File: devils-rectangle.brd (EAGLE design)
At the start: 54 x 54 mm, 26 parts, among them J3 CORTEX_DEBUG_PTH, J6 USB-MICROB, U1 ATSAMD21G-M, U2 MIC5501-3.0YM5-TR, U3 TPD2S017, Y1 32.768KHZ

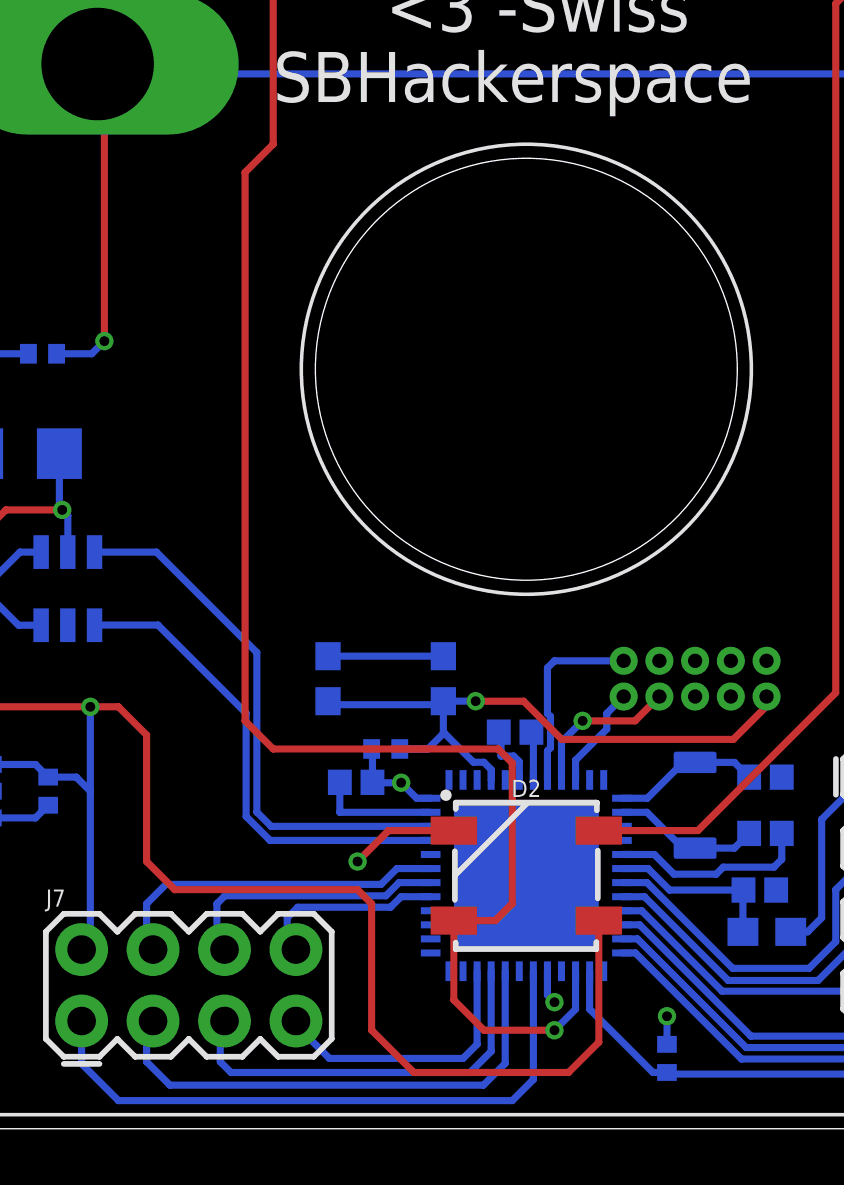
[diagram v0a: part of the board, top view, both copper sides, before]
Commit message: resolved routing errors
resolved routing errors, added crystal, and tested. submitted to oshpark.
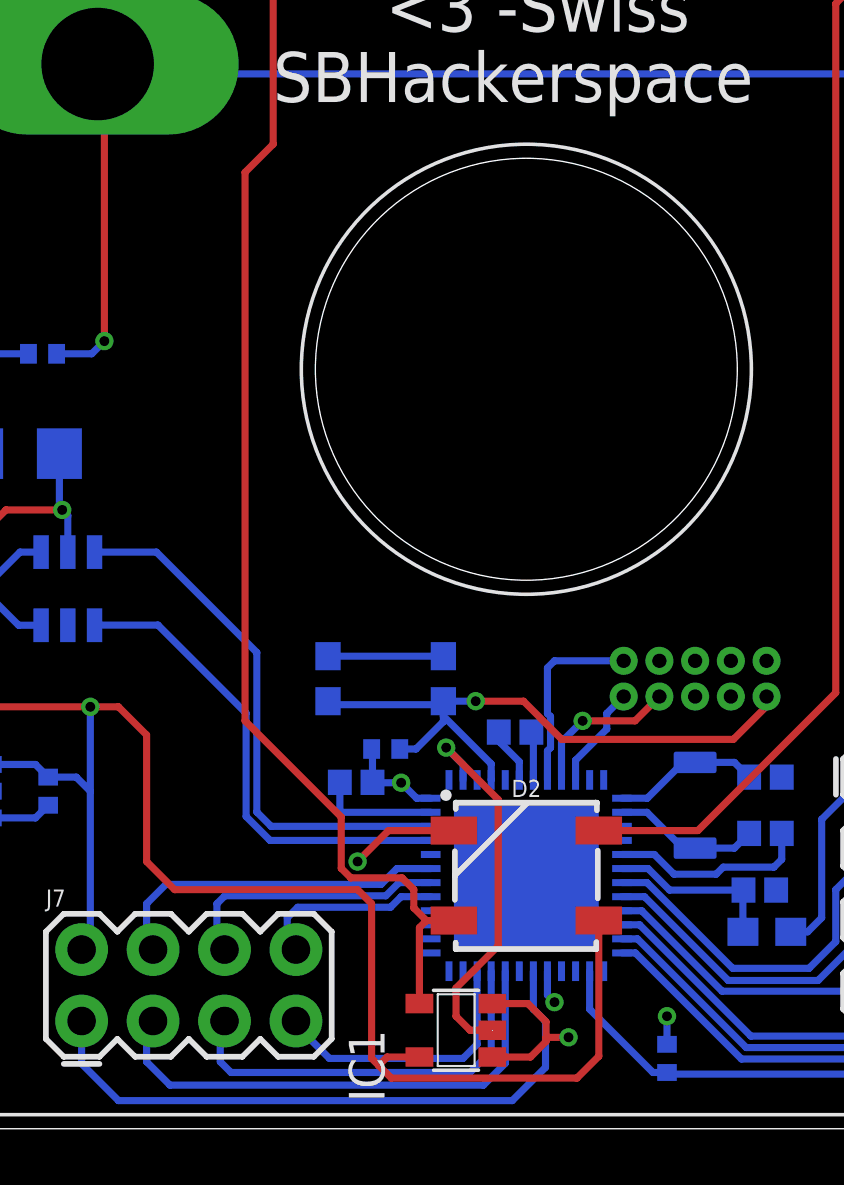
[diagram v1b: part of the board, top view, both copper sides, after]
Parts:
- added IC1: 74AHC1G125DBV, 74xx-custom:SOT23-5
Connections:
- new net DI: D2.4, IC1.4, J1.2
- net 5V: now also IC1.5
- net DIO: now also IC1.2, U1.38; no longer D2.4, J1.2, U1.15
- net GND: now also IC1.1, IC1.3
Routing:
- net DI: track 0.00 -> 54.0 mm, vias 0 -> 1
- net DIO: track 65.8 -> 13.8 mm, vias 2 -> 1
- net GND: track 56.1 -> 62.1 mm, vias 11 -> 12
- net 5V: track 132.5 -> 135.1 mm

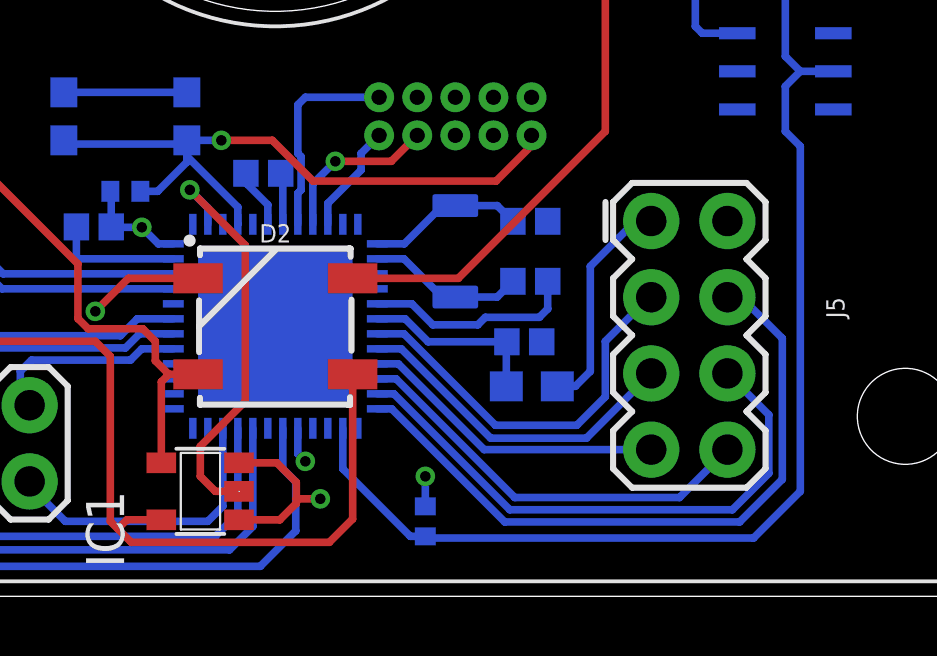
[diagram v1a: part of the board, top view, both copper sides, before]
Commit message: sent to fab
sent to fab, errors on board
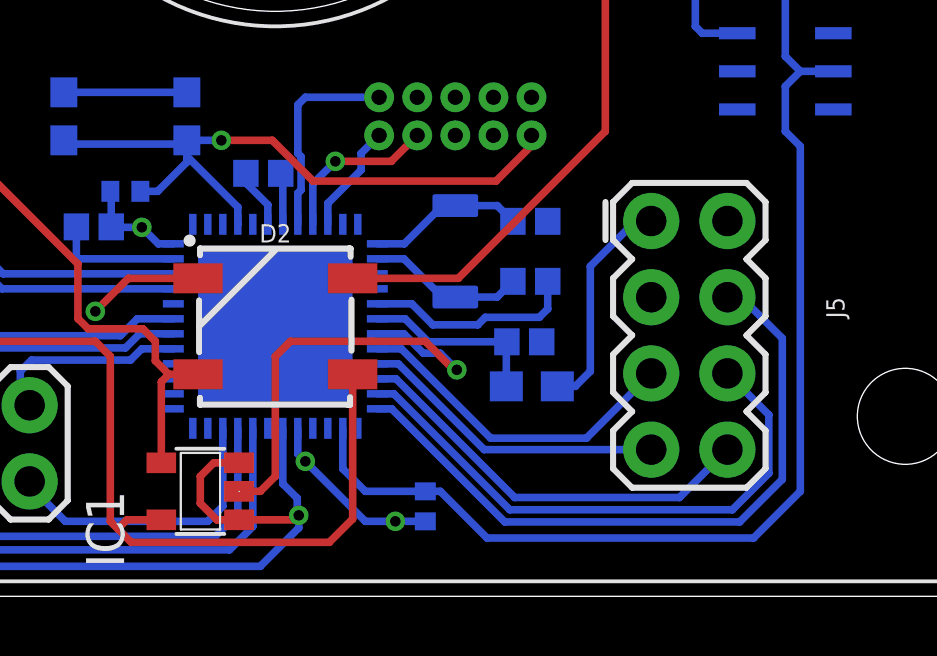
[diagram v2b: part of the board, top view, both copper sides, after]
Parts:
- moved R2 0.50 mm to (32.0, 3.00), turned to 270 degrees
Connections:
- net DIO: now also U1.7; no longer U1.38
- net PA08: no longer U1.7
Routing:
- net PA08: track 13.2 -> 0.06 mm
- net VCC: track 23.2 -> 27.1 mm
- net DIO: track 13.8 -> 15.3 mm
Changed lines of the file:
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@@
 </element>
 <element name="C3" library="SparkFun-Capacitors" library_urn="urn:adsk.eagle:library:510" package="0402" package3d_urn="urn:adsk.eagle:package:37413/1" value=".1uF" x="35.3" y="8.485" smashed="yes" rot="MR180">
-<attribute name="NAME" x="32.911" y="8.223" size="0.6096" layer="26" rot="MR180"/>
+<attribute name="NAME" x="36.911" y="8.723" size="0.6096" layer="26" rot="MR180"/>
 <attribute name="PROD_ID" value="CAP-12416" x="35.3" y="8.485" size="1.778" layer="28" rot="MR180" display="off"/>
 <attribute name="VALUE" value="0.1uF" x="31.961" y="9.217" size="0.6096" layer="26" rot="MR180"/>
@@
 <attribute name="PROD_ID" value="SWCH-13065" x="22" y="16" size="1.778" layer="28" rot="MR180" display="off"/>
 </element>
-<element name="R2" library="rcl" library_urn="urn:adsk.eagle:library:334" package="R0402" package3d_urn="urn:adsk.eagle:package:23547/2" value="4.7k" x="32" y="2.5" smashed="yes" rot="MR90">
-<attribute name="NAME" x="32.635" y="1.865" size="0.8128" layer="26" rot="MR90"/>
-<attribute name="SPICEPREFIX" value="R" x="32" y="2.5" size="1.778" layer="28" rot="MR90" display="off"/>
-<attribute name="VALUE" x="30.595" y="1.865" size="0.8128" layer="26" rot="MR90"/>
+<element name="R2" library="rcl" library_urn="urn:adsk.eagle:library:334" package="R0402" package3d_urn="urn:adsk.eagle:package:23547/2" value="4.7k" x="32" y="3" smashed="yes" rot="MR270">
+<attribute name="NAME" x="31.365" y="4.635" size="0.8128" layer="26" rot="MR270"/>
+<attribute name="SPICEPREFIX" value="R" x="32" y="3" size="1.778" layer="28" rot="MR270" display="off"/>
+<attribute name="VALUE" x="33.405" y="3.635" size="0.8128" layer="26" rot="MR270"/>
 </element>
 <element name="F1" library="SparkFun-Fuses" library_urn="urn:adsk.eagle:library:517" package="1206" package3d_urn="urn:adsk.eagle:package:38575/1" value="6V/0.5A" x="9" y="24" smashed="yes" rot="MR180">
@@
 <contactref element="IC1" pad="3"/>
 <contactref element="IC1" pad="1"/>
-<wire x1="27.25" y1="5.6" x2="27.25" y2="4.25" width="0.254" layer="16"/>
-<wire x1="27.6814" y1="3.8186" x2="27.6814" y2="2.1814" width="0.254" layer="16"/>
-<wire x1="27.25" y1="4.25" x2="27.6814" y2="3.8186" width="0.254" layer="16"/>
-<wire x1="27.6814" y1="2.1814" x2="26.5" y2="1" width="0.254" layer="16"/>
-<wire x1="25.79" y1="2.55" x2="27.15" y2="2.55" width="0.254" layer="1"/>
-<wire x1="27.15" y1="2.55" x2="27.7" y2="3.1" width="0.254" layer="1"/>
-<wire x1="27.7" y1="3.1" x2="27.7" y2="3.25" width="0.254" layer="1"/>
-<wire x1="27.7" y1="3.25" x2="27.7" y2="3.8" width="0.254" layer="1"/>
-<wire x1="27.7" y1="3.8" x2="27.05" y2="4.45" width="0.254" layer="1"/>
-<wire x1="27.05" y1="4.45" x2="25.79" y2="4.45" width="0.254" layer="1"/>
-<via x="28.5" y="3.25" extent="1-16" drill="0.35"/>
-<wire x1="28.5" y1="3.25" x2="27.7" y2="3.25" width="0.254" layer="1"/>
+<wire x1="27.25" y1="5.6" x2="27.25" y2="3.75" width="0.254" layer="16"/>
+<wire x1="27.7314" y1="3.2686" x2="27.7314" y2="2.75" width="0.254" layer="16"/>
+<wire x1="27.7314" y1="2.75" x2="27.7814" y2="2.7" width="0.254" layer="16"/>
+<wire x1="27.7814" y1="2.7" x2="27.7814" y2="2.2814" width="0.254" layer="16"/>
+<wire x1="27.25" y1="3.75" x2="27.7314" y2="3.2686" width="0.254" layer="16"/>
+<wire x1="27.7814" y1="2.2814" x2="26.5" y2="1" width="0.254" layer="16"/>
+<wire x1="25.79" y1="4.45" x2="24.95" y2="4.45" width="0.254" layer="1"/>
+<wire x1="24.95" y1="4.45" x2="24.5" y2="4" width="0.254" layer="1"/>
+<wire x1="24.5" y1="4" x2="24.5" y2="3.1" width="0.254" layer="1"/>
+<wire x1="24.5" y1="3.1" x2="25.05" y2="2.55" width="0.254" layer="1"/>
+<wire x1="25.05" y1="2.55" x2="25.79" y2="2.55" width="0.254" layer="1"/>
+<wire x1="27.7814" y1="2.7" x2="27.6314" y2="2.55" width="0.254" layer="1"/>
+<wire x1="27.6314" y1="2.55" x2="25.79" y2="2.55" width="0.254" layer="1"/>
+<via x="27.7814" y="2.7" extent="1-16" drill="0.35"/>
 </signal>
 <signal name="1W">
@@
 <contactref element="J2" pad="2"/>
 <wire x1="29.25" y1="5.6" x2="29.25" y2="4.25" width="0.254" layer="16"/>
-<wire x1="29.25" y1="4.25" x2="31.5" y2="2" width="0.254" layer="16"/>
-<wire x1="31.5" y1="2" x2="32" y2="2" width="0.254" layer="16"/>
+<wire x1="29.25" y1="4.25" x2="30" y2="3.5" width="0.254" layer="16"/>
+<wire x1="30" y1="3.5" x2="32" y2="3.5" width="0.254" layer="16"/>
 <wire x1="48.3" y1="42.5" x2="44.5" y2="42.5" width="0.254" layer="16"/>
 <wire x1="44.5" y1="42.5" x2="5.7" y2="42.5" width="0.254" layer="16"/>
@@
 <wire x1="44" y1="17" x2="44.5" y2="17.5" width="0.254" layer="16"/>
 <wire x1="44.5" y1="17.5" x2="45.6002" y2="17.5" width="0.254" layer="16"/>
-<wire x1="42.943" y1="1.943" x2="32.057" y2="1.943" width="0.254" layer="16"/>
-<wire x1="32" y1="2" x2="32.057" y2="1.943" width="0.254" layer="16"/>
+<wire x1="42.943" y1="1.943" x2="34.057" y2="1.943" width="0.254" layer="16"/>
+<wire x1="34.057" y1="1.943" x2="32.5" y2="3.5" width="0.254" layer="16"/>
+<wire x1="32" y1="3.5" x2="32.5" y2="3.5" width="0.254" layer="16"/>
 <wire x1="44.5" y1="3.5" x2="42.943" y2="1.943" width="0.254" layer="16"/>
 <wire x1="44" y1="15.5" x2="44.5" y2="15" width="0.254" layer="16"/>
@@
 <vertex x="0.5" y="0.5"/>
 </polygon>
-<via x="32" y="4" extent="1-16" drill="0.35"/>
+<via x="31" y="2.5" extent="1-16" drill="0.35"/>
 <via x="28" y="4.5" extent="1-16" drill="0.35"/>
 <wire x1="27.75" y1="5.6" x2="27.75" y2="4.75" width="0.254" layer="16"/>
 <wire x1="27.75" y1="4.75" x2="28" y2="4.5" width="0.254" layer="16"/>
 <contactref element="R2" pad="2"/>
-<wire x1="32" y1="4" x2="32" y2="3" width="0.254" layer="16"/>
+<wire x1="31" y1="2.5" x2="32" y2="2.5" width="0.254" layer="16"/>
 <contactref element="U1" pad="44"/>
 <contactref element="C2" pad="1"/>
@@
 <wire x1="27.859" y1="14.6552125" x2="27.75" y2="14.7642125" width="0.254" layer="16"/>
 <wire x1="27.75" y1="14.7642125" x2="27.75" y2="16.385" width="0.254" layer="16"/>
+<wire x1="28" y1="4.5" x2="30" y2="2.5" width="0.254" layer="16"/>
+<wire x1="30" y1="2.5" x2="31" y2="2.5" width="0.254" layer="16"/>
 </signal>
 <signal name="N$4">
@@
 <signal name="DIO">
 <contactref element="IC1" pad="2"/>
-<contactref element="U1" pad="38"/>
-<wire x1="24.75" y1="12.4" x2="24.75" y2="12.95" width="0.254" layer="16"/>
-<wire x1="24.75" y1="12.95" x2="24.15" y2="13.55" width="0.254" layer="16"/>
-<via x="24.15" y="13.55" extent="1-16" drill="0.35"/>
-<wire x1="24.15" y1="13.55" x2="26" y2="11.7" width="0.254" layer="1"/>
-<wire x1="26" y1="6.5" x2="24.5" y2="5" width="0.254" layer="1"/>
-<wire x1="24.5" y1="5" x2="24.5" y2="4" width="0.254" layer="1"/>
-<wire x1="24.5" y1="4" x2="25" y2="3.5" width="0.254" layer="1"/>
-<wire x1="25" y1="3.5" x2="25.79" y2="3.5" width="0.254" layer="1"/>
-<wire x1="26" y1="11.7" x2="26" y2="6.5" width="0.254" layer="1"/>
+<contactref element="U1" pad="7"/>
+<wire x1="25.79" y1="3.5" x2="26.5" y2="3.5" width="0.254" layer="1"/>
+<wire x1="26.5" y1="3.5" x2="27" y2="4" width="0.254" layer="1"/>
+<wire x1="27" y1="4" x2="27" y2="8" width="0.254" layer="1"/>
+<wire x1="27" y1="8" x2="27.5" y2="8.5" width="0.254" layer="1"/>
+<wire x1="27.5" y1="8.5" x2="32" y2="8.5" width="0.254" layer="1"/>
+<wire x1="32" y1="8.5" x2="33" y2="7.5" width="0.254" layer="1"/>
+<wire x1="33" y1="7.5" x2="33.05" y2="7.55" width="0.254" layer="1"/>
+<via x="33.05" y="7.55" extent="1-16" drill="0.35"/>
+<wire x1="33.05" y1="7.55" x2="32.496" y2="8.104" width="0.254" layer="16"/>
+<wire x1="32.496" y1="8.104" x2="31.93481875" y2="8.104" width="0.254" layer="16"/>
+<wire x1="31.28881875" y1="8.75" x2="30.4" y2="8.75" width="0.254" layer="16"/>
+<wire x1="31.93481875" y1="8.104" x2="31.28881875" y2="8.75" width="0.254" layer="16"/>
 </signal>
 <signal name="DO">
@@
 </signal>
 <signal name="PA08">
-<contactref element="U1" pad="7"/>
 <contactref element="J5" pad="3"/>
-<wire x1="34.33681875" y1="5.702" x2="37.05" y2="5.702" width="0.254" layer="16"/>
-<wire x1="37.05" y1="5.702" x2="38" y2="6.652" width="0.254" layer="16"/>
-<wire x1="38" y1="6.652" x2="38" y2="8.5" width="0.254" layer="16"/>
-<wire x1="38" y1="8.5" x2="39.47" y2="9.97" width="0.254" layer="16"/>
 <wire x1="39.47" y1="9.97" x2="39.53" y2="9.97" width="0.254" layer="16"/>
-<wire x1="30.4" y1="8.75" x2="31.28881875" y2="8.75" width="0.254" layer="16"/>
-<wire x1="31.28881875" y1="8.75" x2="34.33681875" y2="5.702" width="0.254" layer="16"/>
 </signal>
 <signal name="PA09">
